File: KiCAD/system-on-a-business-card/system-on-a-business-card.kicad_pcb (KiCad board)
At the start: 2 copper layers, 85 x 55 mm, 105 parts, among them J1 USB_C_Receptacle, J2 X077-6428TSWCG01-H13, Q1 2N7002K, Q10 2N7002K, Q11 2N7002K, Q12 2N7002K, Q2 BSS84, Q3 2N7002K, Q4 2N7002K, Q5 2N7002K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

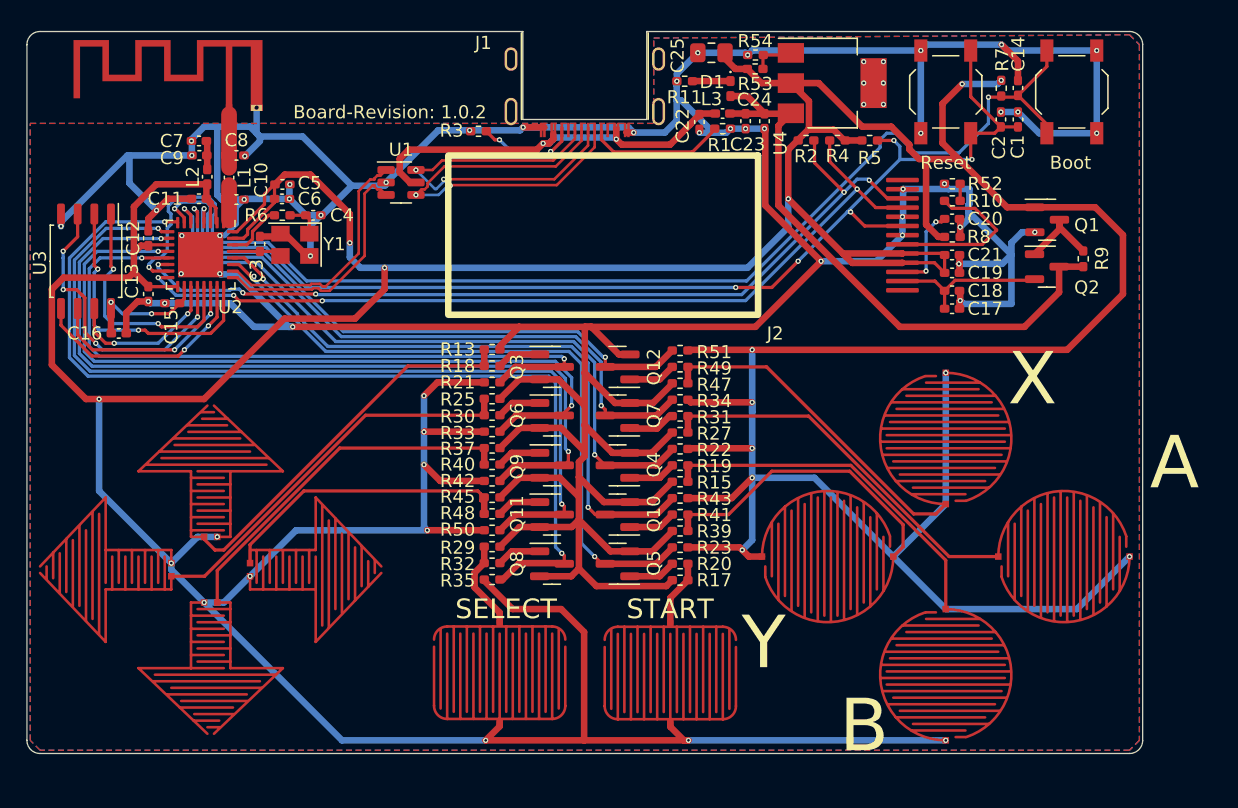
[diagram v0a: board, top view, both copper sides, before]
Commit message: #10: removed on/off switch again, started working on layout
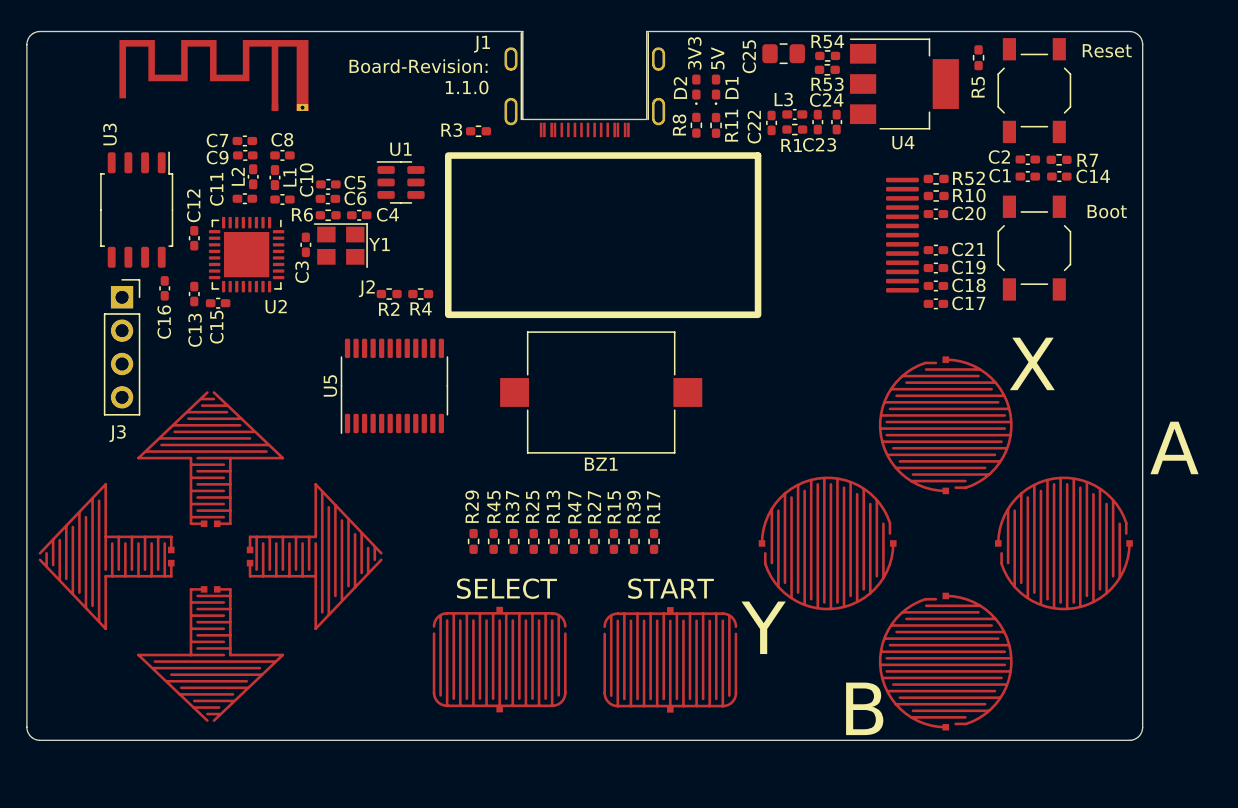
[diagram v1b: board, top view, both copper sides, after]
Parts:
- removed Q1, Q10, Q11, Q12, Q3, Q4, Q5, Q6, Q7, Q8, Q9: 2N7002K, Package_TO_SOT_SMD:SOT-23
- removed Q2: BSS84, Package_TO_SOT_SMD:SOT-23
- removed R18, R19, R20, R21, R22, R23, R30, R31, R32, R33, R34, R35, R40, R41, R42, R43, R48, R49, R50, R51: 10k, Resistor_SMD:R_0402_1005Metric_Pad0.72x0.64mm_HandSolder
- removed R9: 47k, Resistor_SMD:R_0402_1005Metric_Pad0.72x0.64mm_HandSolder
- added BZ1: Buzzer, Buzzer_Beeper:Buzzer_Mallory_AST1109MLTRQ, F.Cu at (121.2, 97.5)
- added D2: LED, Diode_SMD:D_0402_1005Metric_Pad0.77x0.64mm_HandSolder, F.Cu at (128.5, 74.2)
- added J3: Conn_01x04_Socket, Connector_PinSocket_2.54mm:PinSocket_1x04_P2.54mm_Vertical, F.Cu at (84.8, 90.2)
- added U5: TCA9535PWR, Package_SO:TSSOP-24_4.4x7.8mm_P0.65mm, F.Cu at (105.5, 97.0)
- R53: value 8k25 -> 121
- R54: value 10k -> 75
- moved R2 33.8 mm to (105.1, 90.0)
- moved R4 33.8 mm to (107.5, 90.0)
- moved R8 21.3 mm to (128.5, 77.1), turned to -90 degrees
- moved R13 15.4 mm to (117.6, 108.8), turned to -90 degrees
- moved R47 14.5 mm to (119.2, 108.8), turned to -90 degrees
- moved SW2 12.2 mm to (154.2, 86.5)
- moved R25 11.3 mm to (116.1, 108.8), turned to -90 degrees
- moved R27 10.6 mm to (120.7, 108.8), turned to -90 degrees
- moved R5 10.4 mm to (150.0, 72.0), turned to 90 degrees
- moved C14 7.45 mm to (156.2, 81.0), turned to 0 degrees
- moved R37 7.30 mm to (114.6, 108.8), turned to -90 degrees
- moved R7 7.02 mm to (156.1, 79.8), turned to 180 degrees
- moved R15 6.79 mm to (122.2, 108.8), turned to -90 degrees
- moved SW1 6.75 mm to (154.2, 74.5)
- moved C22 5.50 mm to (134.2, 77.0)
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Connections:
- net Net-(R12-Pad1) renamed UP
- net Net-(R14-Pad2) renamed B
- net Net-(R16-Pad1) renamed START
- net Net-(R24-Pad1) renamed LEFT
- net Net-(R26-Pad2) renamed A
- net Net-(R28-Pad1) renamed SELECT
- net Net-(R36-Pad1) renamed DOWN
- net Net-(R38-Pad2) renamed Y
- net Net-(R44-Pad1) renamed RIGHT
- net Net-(R46-Pad2) renamed X
- C17 pad 1: Net-(J2-Pin_2) -> +5V
- C18 pad 1: Net-(J2-Pin_2) -> +5V
- J2 pad 2: Net-(J2-Pin_2) -> +5V
- J2 pad 8: RESET -> /Display Circuit/RESET_DISPLAY
- R8 pad 1: +3.3V -> Net-(D2-K)
- U2 pad 10: /Host/PAD_DOWN -> /Host/IO_EXP_INT
- U2 pad 12: /Host/PAD_LEFT -> /Display Circuit/RESET_DISPLAY
- U2 pad 13: /Host/PAD_UP -> Net-(BZ1--)
- U2 pad 27: /Host/START -> UART_RXD
- U2 pad 28: /Host/PAD_Y -> UART_TXD
- U2 pad 4: /Host/PAD_X -> unconnected-(U2-XTAL_32K_P/ADC1_CH0-Pad4)
- U2 pad 5: /Host/PAD_A -> unconnected-(U2-XTAL_32K_N/ADC1_CH1-Pad5)
- U2 pad 6: /Host/PAD_B -> unconnected-(U2-GPIO2/ADC1_CH2-Pad6)
- U2 pad 8: /Host/SELECT -> unconnected-(U2-GPIO3/ADC1_CH3-Pad8)
- U2 pad 9: /Host/PAD_RIGHT -> unconnected-(U2-MTMS/GPIO4/ADC1_CH4-Pad9)
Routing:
- net +3.3V: track 497.9 -> 0.00 mm, vias 24 -> 0
- net GND: track 390.7 -> 0.00 mm, vias 50 -> 0
- net BOOT: track 92.7 -> 0.00 mm, vias 2 -> 0
- net RESET: track 91.2 -> 0.00 mm, vias 6 -> 0
- net /Host/SELECT: track 74.3 -> 0.00 mm, vias 2 -> 0
- net /Host/PAD_RIGHT: track 69.1 -> 0.00 mm, vias 2 -> 0
- net /Display Circuit/SDA: track 67.8 -> 0.00 mm, vias 5 -> 0
- net /Display Circuit/SCL: track 66.9 -> 0.00 mm, vias 4 -> 0
- net /Host/PAD_DOWN: track 64.6 -> 0.00 mm, vias 2 -> 0
- net /Host/PAD_LEFT: track 60.0 -> 0.00 mm, vias 2 -> 0
- net /Host/PAD_UP: track 54.9 -> 0.00 mm, vias 2 -> 0
- net /Host/PAD_B: track 52.9 -> 0.00 mm, vias 2 -> 0
- net /Host/START: track 51.4 -> 0.00 mm, vias 2 -> 0
- net /Host/PAD_Y: track 48.8 -> 0.00 mm, vias 2 -> 0
- net /Host/PAD_A: track 48.7 -> 0.00 mm, vias 2 -> 0
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- removed copper zone on B.Cu, net GND
- removed copper zone on F.Cu, net GND
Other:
- board size 85 x 55 mm -> 85 x 54 mm
- copper layers 2 -> 4
- board text added: "3V3"
- board text added: "5V"
- board text added: "Board-Revision: 1.1.0"
- board text removed: "Board-Revision: 1.0.2"

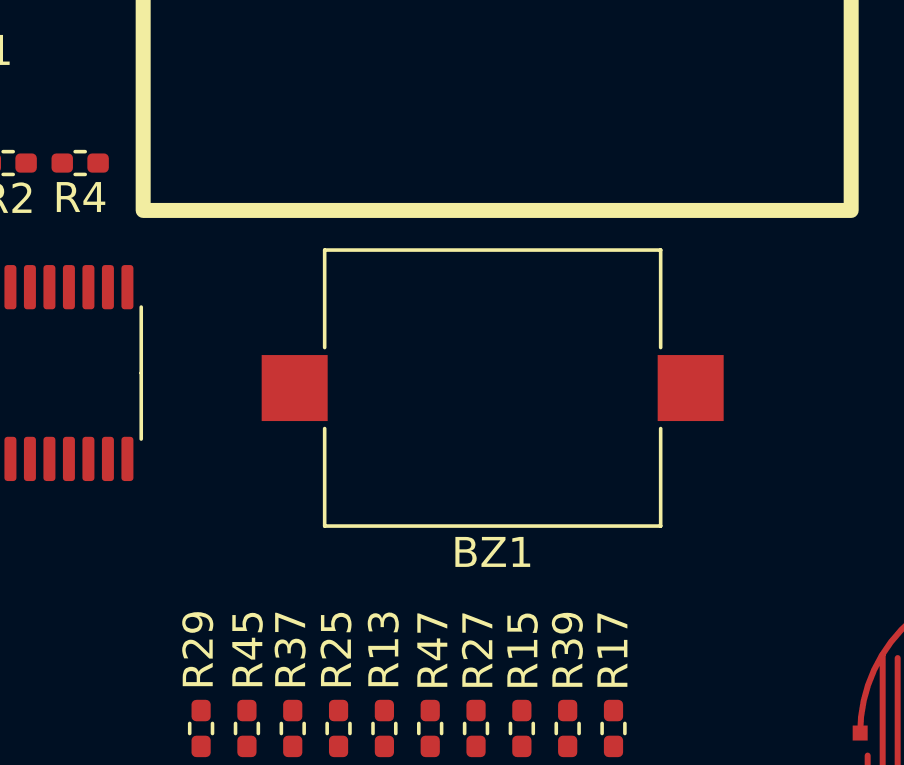
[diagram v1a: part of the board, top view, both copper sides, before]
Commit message: #10: updated buzzer circuit
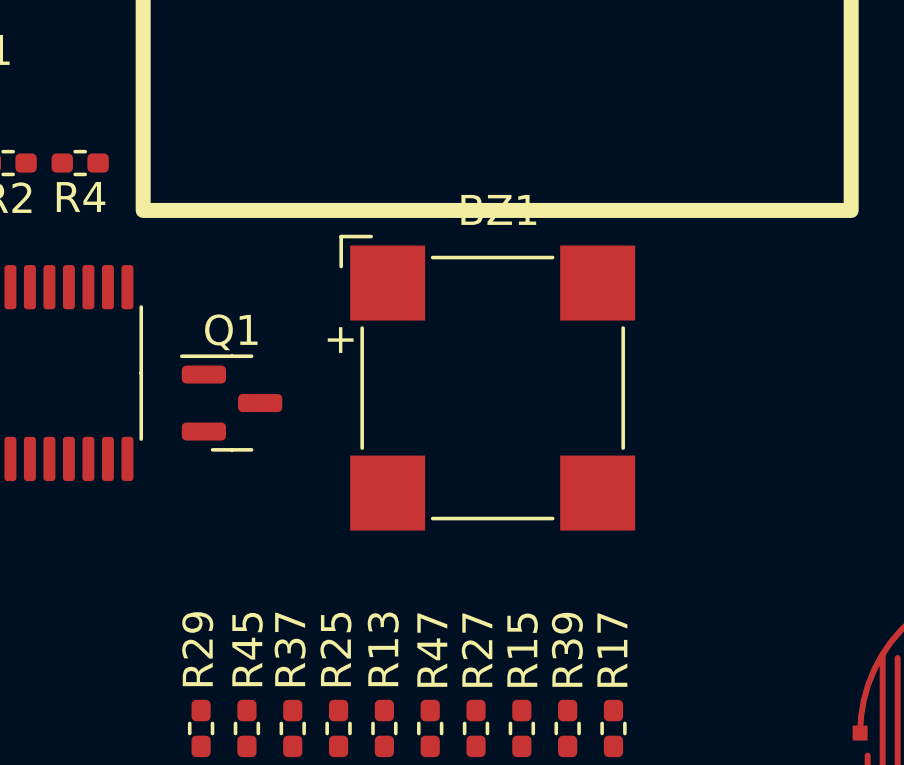
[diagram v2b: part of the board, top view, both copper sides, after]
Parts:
- added Q1: 2N7002K, Package_TO_SOT_SMD:SOT-23, F.Cu at (112.6, 98.0)
- BZ1: footprint Buzzer_Beeper:Buzzer_Mallory_AST1109MLTRQ -> Buzzer_Beeper:MagneticBuzzer_CUI_CMT-8504-100-SMT
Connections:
- BZ1 pad 1: Net-(BZ1--) -> +3.3V
- BZ1 pad 2: GND -> Net-(BZ1-+)
- U2 pad 13: Net-(BZ1--) -> BUZZER

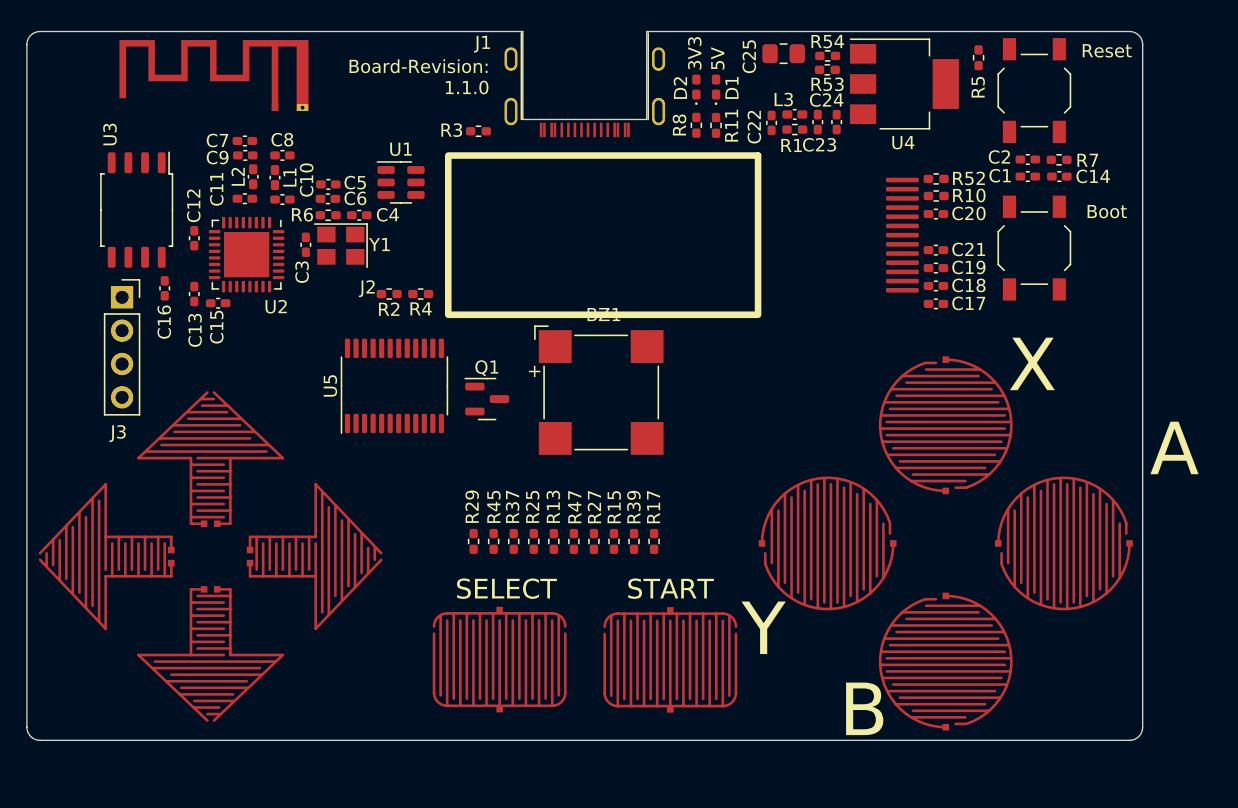
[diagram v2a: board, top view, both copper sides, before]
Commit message: #10: continued layouting, added 2nd buzzer
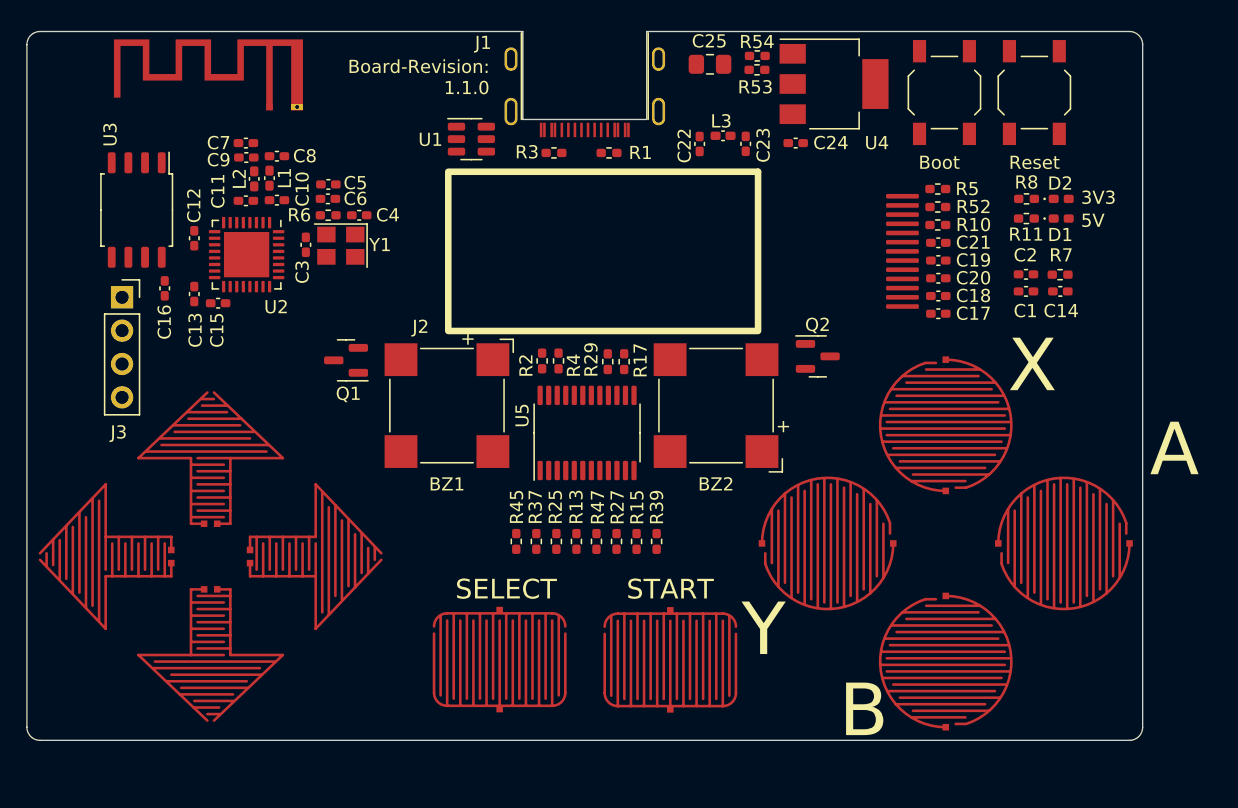
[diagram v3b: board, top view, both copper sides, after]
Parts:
- added BZ2: Buzzer, Buzzer_Beeper:MagneticBuzzer_CUI_CMT-8504-100-SMT, F.Cu at (130.0, 98.5)
- added Q2: 2N7002K, Package_TO_SOT_SMD:SOT-23, F.Cu at (137.8, 94.8)
- moved D2 29.1 mm to (156.3, 82.8), turned to 0 degrees
- moved D1 28.1 mm to (156.3, 84.2), turned to 0 degrees
- moved R8 25.8 mm to (153.7, 82.8), turned to 180 degrees
- moved R11 24.7 mm to (153.6, 84.2), turned to 180 degrees
- moved R29 17.1 mm to (121.8, 95.2), turned to 90 degrees
- moved U5 15.1 mm to (120.2, 100.6)
- moved R1 14.3 mm to (121.8, 79.2)
- moved R17 13.9 mm to (123.0, 95.2), turned to 90 degrees
- moved SW2 13.7 mm to (147.4, 74.7)
- moved R2 12.7 mm to (116.8, 95.1), turned to -90 degrees
- moved BZ1 11.8 mm to (109.5, 98.5), turned to -90 degrees
- moved R4 11.7 mm to (118.0, 95.1), turned to -90 degrees
- moved Q1 11.1 mm to (101.8, 95.0), turned to 180 degrees
- moved R5 10.5 mm to (146.9, 82.0), turned to 0 degrees
- moved C1 8.75 mm to (153.6, 89.8)
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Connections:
- Q1 pad 1: BUZZER -> BUZZER_L
- U2 pad 12: /Display Circuit/RESET_DISPLAY -> BUZZER_L
- U2 pad 13: BUZZER -> BUZZER_R
- U2 pad 9: unconnected-(U2-MTMS/GPIO4/ADC1_CH4-Pad9) -> /Display Circuit/RESET_DISPLAY
- U5 pad 10: X -> A
- U5 pad 11: Y -> B
- U5 pad 4: UP -> RIGHT
- U5 pad 5: LEFT -> DOWN
- U5 pad 6: DOWN -> LEFT
- U5 pad 7: RIGHT -> UP
- U5 pad 8: A -> X
- U5 pad 9: B -> Y

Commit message: #10: started with routing
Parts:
- added FID1: Fiducial, Fiducial:Fiducial_1mm_Mask2mm, F.Cu at (158.5, 76.8)
- added FID2: Fiducial, Fiducial:Fiducial_1mm_Mask2mm, F.Cu at (158.6, 120.1)
- added FID3: Fiducial, Fiducial:Fiducial_1mm_Mask2mm, F.Cu at (81.5, 76.8)
- added FID4: Fiducial, Fiducial:Fiducial_1mm_Mask2mm, F.Cu at (81.5, 120.0)
- J3: footprint Connector_PinSocket_2.54mm:PinSocket_1x04_P2.54mm_Vertical -> Prj_connectors:solder_pads_4x1; moved to B.Cu
- moved J3 50.4 mm to (123.3, 122.8), turned to 90 degrees
- moved C14 8.49 mm to (152.0, 82.4), turned to -90 degrees
- moved C1 7.64 mm to (155.6, 82.4), turned to -90 degrees
- moved R5 7.48 mm to (154.4, 82.4), turned to 90 degrees
- moved C2 6.87 mm to (156.8, 82.4), turned to -90 degrees
- moved R7 6.78 mm to (153.2, 82.4), turned to 90 degrees
- moved D1 6.65 mm to (156.2, 90.9)
- moved D2 6.65 mm to (156.2, 89.4)
- moved R11 6.65 mm to (153.5, 90.9)
- moved R8 6.65 mm to (153.5, 89.4)
- moved R47 4.61 mm to (125.5, 108.8)
- moved R13 4.58 mm to (114.8, 108.8)
- moved R37 3.07 mm to (119.4, 108.8)
- moved R15 3.04 mm to (120.9, 108.8)
- moved R39 3.04 mm to (122.4, 108.8)
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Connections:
- J3 pad 2: UART_RXD -> UART_TXD
- J3 pad 3: UART_TXD -> UART_RXD
- U2 pad 12: BUZZER_L -> BUZZER_R
- U2 pad 13: BUZZER_R -> BUZZER_L
- U5 pad 11: B -> X
- U5 pad 4: RIGHT -> UP
- U5 pad 5: DOWN -> RIGHT
- U5 pad 7: UP -> DOWN
- U5 pad 8: X -> B
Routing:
- net RESET: track 0.00 -> 89.0 mm, vias 0 -> 2
- net BOOT: track 0.00 -> 83.7 mm, vias 0 -> 2
- net /Display Circuit/SDA: track 0.00 -> 69.5 mm, vias 0 -> 2
- net /Display Circuit/SCL: track 0.00 -> 67.8 mm, vias 0 -> 2
- net UART_RXD: track 0.00 -> 64.8 mm, vias 0 -> 1
- net UART_TXD: track 0.00 -> 63.1 mm, vias 0 -> 1
- net /Display Circuit/RESET_DISPLAY: track 0.00 -> 62.3 mm, vias 0 -> 2
- net /Host/IO_EXP_INT: track 0.00 -> 52.8 mm, vias 0 -> 2
- net BUZZER_R: track 0.00 -> 51.4 mm, vias 0 -> 2
- net LEFT: track 0.00 -> 41.1 mm
- net A: track 0.00 -> 39.6 mm
- net DOWN: track 0.00 -> 39.0 mm
- net B: track 0.00 -> 36.9 mm
- net RIGHT: track 0.00 -> 36.3 mm
- net +3.3V: track 0.00 -> 35.9 mm
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- added copper zone on B.Cu, net GND
- added copper zone on F.Cu, net GND
- added copper zone on In1.Cu, net GND
- added copper zone on In2.Cu, net GND
